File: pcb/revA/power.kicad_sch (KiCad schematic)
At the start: 24 parts, among them J5 5V_PRG, U13 1117-3.3, U14 1117-3.3, U15 1117-1.2

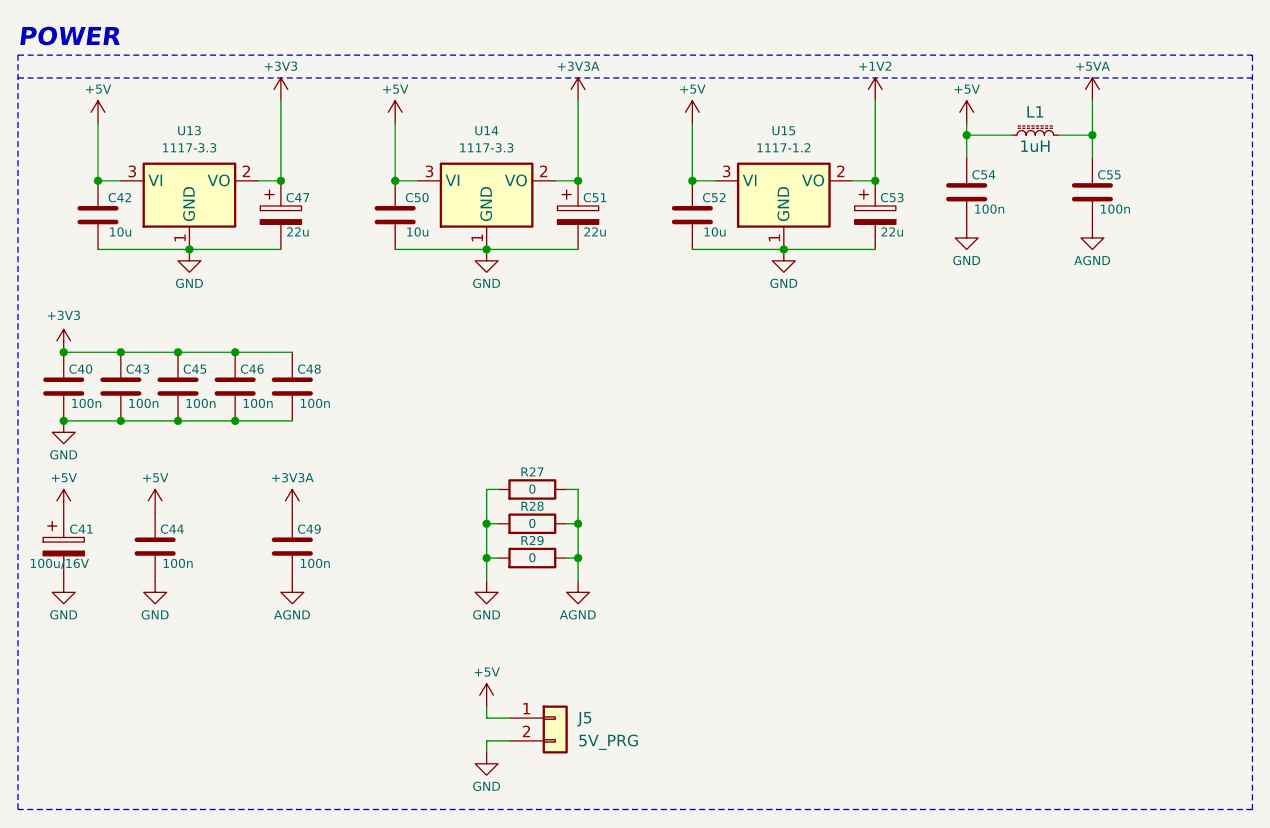
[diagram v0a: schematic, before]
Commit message: Updated gerbers to min 0.2/0.45 vias, firmware build for xc6slx16
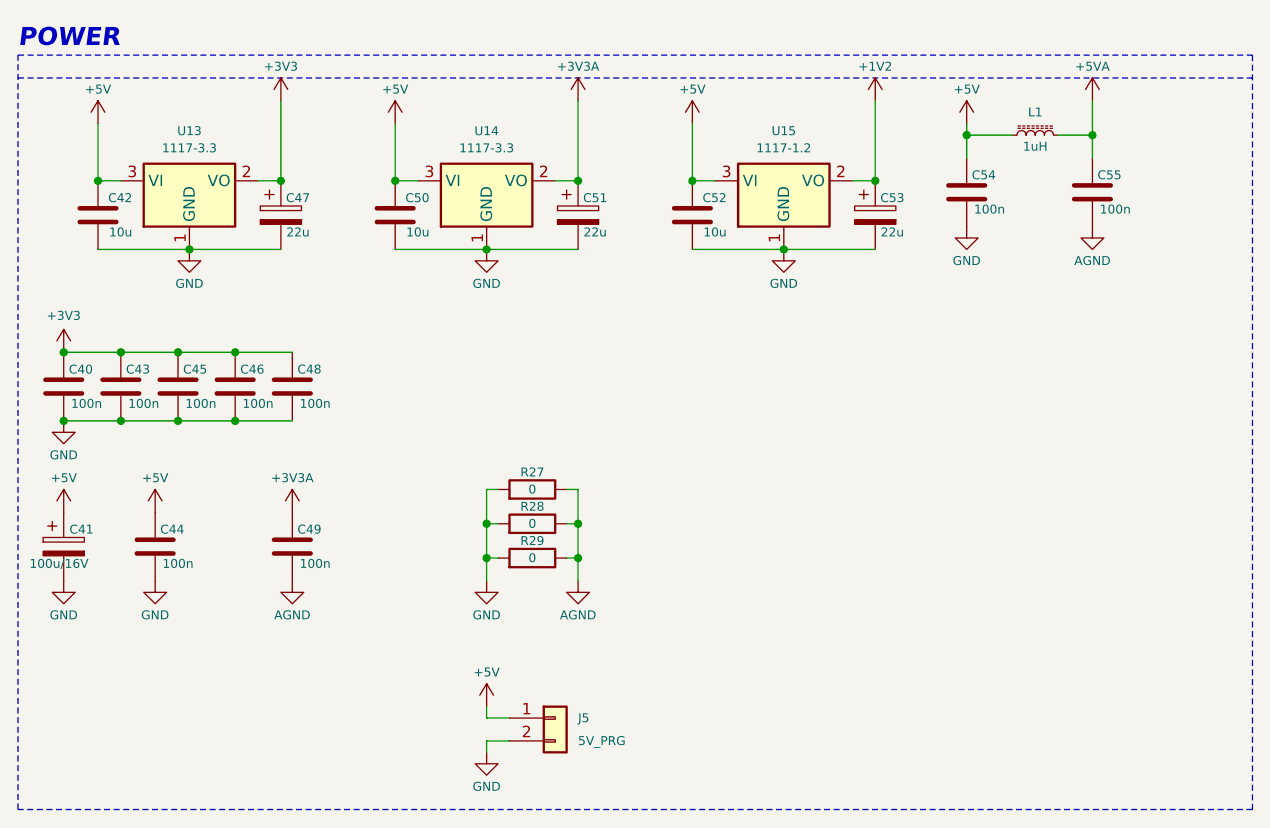
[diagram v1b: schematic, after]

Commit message: Updated revA (cosmetic changes)
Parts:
- J5: now not fitted
- R28, R29: now not fitted; now left out of the parts list
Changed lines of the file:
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@@
 		(on_board yes)
 		(in_pos_files yes)
-		(dnp no)
+		(dnp yes)
 		(fields_autoplaced yes)
 		(property "Reference" "J5"
@@
 		(body_style 1)
 		(exclude_from_sim no)
-		(in_bom yes)
-		(on_board yes)
-		(in_pos_files yes)
-		(dnp no)
+		(in_bom no)
+		(on_board yes)
+		(in_pos_files yes)
+		(dnp yes)
 		(property "Reference" "R28"
 			(at 81.28 74.295 90)
@@
 		(body_style 1)
 		(exclude_from_sim no)
-		(in_bom yes)
-		(on_board yes)
-		(in_pos_files yes)
-		(dnp no)
+		(in_bom no)
+		(on_board yes)
+		(in_pos_files yes)
+		(dnp yes)
 		(property "Reference" "R29"
 			(at 81.28 78.105 90)
